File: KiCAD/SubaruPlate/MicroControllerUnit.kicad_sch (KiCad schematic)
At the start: 1 part, among them U5 XIAO-RP2040-DIP

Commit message: SubaruPlateを更新
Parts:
- added BZ1: Buzzer, symbol Device:Buzzer
- added Q1: NMOS, Package_TO_SOT_SMD:SOT-23, symbol Simulation_SPICE:NMOS
- added R5: 750, Resistor_SMD:R_0603_1608Metric_Pad0.98x0.95mm_HandSolder, symbol Device:R
- added R7: 10k, Resistor_SMD:R_0603_1608Metric_Pad0.98x0.95mm_HandSolder, symbol Device:R
- U5: footprint Module:MOUDLE14P-XIAO-DIP-SMD -> Seeed_XIAO:XIAO-RP2040-SMD
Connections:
- net GND: now also Q1.3 (S), R7.1
- net Servo_PWM: now reaches U5.2 (GPIO27/ADC1/A1)
- net Buzzer: now reaches U5.3 (GPIO28/ADC2/A2)
- net Buzzer: now also R5.1
- new net: Q1.2 (G), R5.2, R7.2
- new net: BZ1.2 (-), Q1.1 (D)
- new net +12V: BZ1.1 (+)
- no-connect marks 5 -> 3
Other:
- note added: "アナデジ太郎の回路設計・FETのゲート・ソース間抵抗の決め方"
- note added: "アナデジ太郎の回路設計・FETゲート抵抗の決め方"

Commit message: 後は最終確認
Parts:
- added R13: 600, Resistor_SMD:R_0603_1608Metric_Pad0.98x0.95mm_HandSolder, symbol Device:R
- BZ1: footprint (none) -> Buzzer_Beeper:Buzzer_12x9.5RM7.6
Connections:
- net +12V: now also R13.1; no longer BZ1.1 (+)
- net SPI_CS_MCP2515: now reaches U5.4 (GPIO29/ADC3/A3)
- net +3.3V: no longer names the net of U5.12 (3V3)
- new net: BZ1.1 (+), R13.2
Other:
- note added: "音質に問題があれば，0Ω抵抗で配線→"
- moved on the sheet: BZ1, Q1, R5, R7

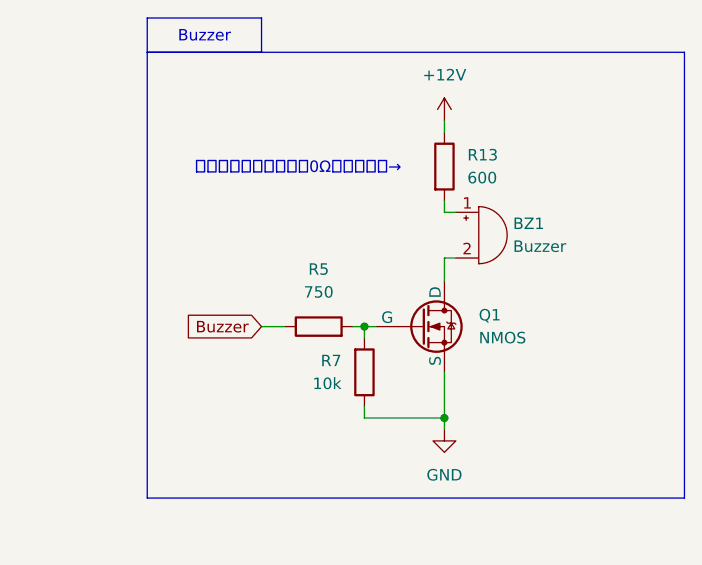
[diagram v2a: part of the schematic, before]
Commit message: 取付穴位置を変更
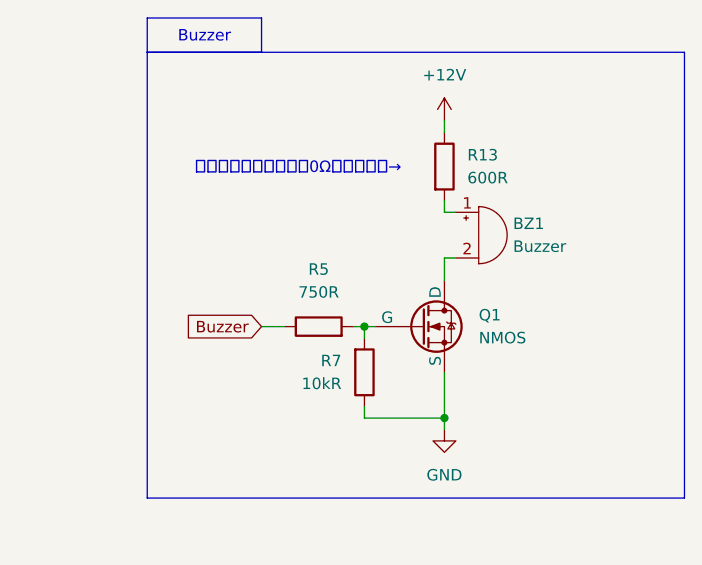
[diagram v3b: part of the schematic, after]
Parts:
- R13: value 600 -> 600R
- R5: value 750 -> 750R
- R7: value 10k -> 10kR
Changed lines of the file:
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@@
 			)
 		)
-		(property "Value" "750"
+		(property "Value" "750R"
 			(at 146.05 52.07 90)
 			(effects
@@
 			)
 		)
-		(property "Value" "600"
+		(property "Value" "600R"
 			(at 162.56 39.3699 0)
 			(effects
@@
 			)
 		)
-		(property "Value" "10k"
+		(property "Value" "10kR"
 			(at 148.59 62.2299 0)
 			(effects

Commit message: ガバーデータ生成
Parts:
- U5: footprint Seeed_XIAO:XIAO-RP2040-SMD -> TSRP_Seeed_XIAO:XIAO-RP2040-SMD
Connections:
- net +12V renamed VIN(12V)
- net SPI_CS: no longer names the net of U5.1 (GPIO26/ADC0/A0)
- net Servo_PWM: no longer names the net of U5.2 (GPIO27/ADC1/A1)
- no-connect marks 3 -> 5
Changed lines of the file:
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@@
+	)
+	(no_connect
+		(at 48.26 36.83)
+	)
+	(no_connect
+		(at 48.26 40.64)
 	)
 	(no_connect
@@
 	(wire
 		(pts
-			(xy 160.02 33.02) (xy 160.02 34.29)
+			(xy 160.02 31.75) (xy 160.02 34.29)
 		)
 		(stroke
@@
 		(pts
 			(xy 151.13 55.88) (xy 151.13 57.15)
+		)
+		(stroke
+			(width 0)
+			(type default)
+		)
+	)
+	(wire
+		(pts
+			(xy 158.75 31.75) (xy 160.02 31.75)
 		)
 		(stroke
@@
 		)
 	)
-	(global_label "Servo_PWM"
-		(shape output)
-		(at 48.26 40.64 180)
+	(global_label "SPI_MISO"
+		(shape input)
+		(at 83.82 52.07 0)
 		(fields_autoplaced yes)
 		(effects
@@
 				(size 1.27 1.27)
 			)
-			(justify right)
+			(justify left)
 		)
 		(property "Intersheetrefs" "${INTERSHEET_REFS}"
-			(at 34.9335 40.64 0)
-			(show_name yes)
-			(effects
-				(font
-					(size 1.27 1.27)
-				)
-				(justify right)
-				(hide yes)
-			)
-		)
-	)
-	(global_label "SPI_MISO"
+			(at 95.4533 52.07 0)
+			(effects
+				(font
+					(size 1.27 1.27)
+				)
+				(justify left)
+				(hide yes)
+			)
+		)
+	)
+	(global_label "I2C_SCL"
 		(shape input)
-		(at 83.82 52.07 0)
+		(at 48.26 55.88 180)
 		(fields_autoplaced yes)
 		(effects
@@
 				(size 1.27 1.27)
 			)
-			(justify left)
+			(justify right)
 		)
 		(property "Intersheetrefs" "${INTERSHEET_REFS}"
-			(at 95.4533 52.07 0)
-			(effects
-				(font
-					(size 1.27 1.27)
-				)
-				(justify left)
-				(hide yes)
-			)
-		)
-	)
-	(global_label "I2C_SCL"
+			(at 37.7153 55.88 0)
+			(effects
+				(font
+					(size 1.27 1.27)
+				)
+				(justify right)
+				(hide yes)
+			)
+		)
+	)
+	(global_label "SPI_CS_MCP2515"
 		(shape input)
-		(at 48.26 55.88 180)
+		(at 48.26 48.26 180)
 		(fields_autoplaced yes)
 		(effects
@@
 		)
 		(property "Intersheetrefs" "${INTERSHEET_REFS}"
-			(at 37.7153 55.88 0)
+			(at 28.9464 48.26 0)
 			(effects
 				(font
@@
 		)
 	)
-	(global_label "SPI_CS_MCP2515"
+	(global_label "I2C_SDA"
 		(shape input)
-		(at 48.26 48.26 180)
+		(at 48.26 52.07 180)
 		(fields_autoplaced yes)
 		(effects
@@
 		)
 		(property "Intersheetrefs" "${INTERSHEET_REFS}"
-			(at 28.9464 48.26 0)
+			(at 37.6548 52.07 0)
 			(effects
 				(font
@@
 		)
 	)
-	(global_label "I2C_SDA"
+	(global_label "Buzzer"
 		(shape input)
-		(at 48.26 52.07 180)
+		(at 139.7 55.88 180)
 		(fields_autoplaced yes)
 		(effects
@@
 		)
 		(property "Intersheetrefs" "${INTERSHEET_REFS}"
-			(at 37.6548 52.07 0)
+			(at 130.3648 55.88 0)
 			(effects
 				(font
@@
 		)
 	)
-	(global_label "Buzzer"
+	(global_label "VIN(12V)"
 		(shape input)
-		(at 139.7 55.88 180)
+		(at 158.75 31.75 180)
 		(fields_autoplaced yes)
 		(effects
@@
 		)
 		(property "Intersheetrefs" "${INTERSHEET_REFS}"
-			(at 130.3648 55.88 0)
-			(effects
-				(font
-					(size 1.27 1.27)
-				)
-				(justify right)
-				(hide yes)
-			)
-		)
-	)
-	(global_label "SPI_CS"
-		(shape input)
-		(at 48.26 36.83 180)
-		(fields_autoplaced yes)
-		(effects
-			(font
-				(size 1.27 1.27)
-			)
-			(justify right)
-		)
-		(property "Intersheetrefs" "${INTERSHEET_REFS}"
-			(at 38.7434 36.83 0)
+			(at 147.5399 31.75 0)
 			(effects
 				(font
@@
 	)
 	(symbol
-		(lib_id "power:+12V")
-		(at 160.02 33.02 0)
-		(unit 1)
-		(exclude_from_sim no)
-		(in_bom yes)
-		(on_board yes)
-		(dnp no)
-		(fields_autoplaced yes)
-		(property "Reference" "#PWR031"
-			(at 160.02 36.83 0)
-			(effects
-				(font
-					(size 1.27 1.27)
-				)
-				(hide yes)
-			)
-		)
-		(property "Value" "+12V"
-			(at 160.02 27.94 0)
-			(effects
-				(font
-					(size 1.27 1.27)
-				)
-			)
-		)
-		(property "Footprint" ""
-			(at 160.02 33.02 0)
-			(effects
-				(font
-					(size 1.27 1.27)
-				)
-				(hide yes)
-			)
-		)
-		(property "Datasheet" ""
-			(at 160.02 33.02 0)
-			(effects
-				(font
-					(size 1.27 1.27)
-				)
-				(hide yes)
-			)
-		)
-		(property "Description" "Power symbol creates a global label with name \"+12V\""
-			(at 160.02 33.02 0)
-			(effects
-				(font
-					(size 1.27 1.27)
-				)
-				(hide yes)
-			)
-		)
-		(pin "1"
-		)
-		(instances
-			(project ""
-				(path "/6c4aa1f5-c08b-4349-85f8-88bb399e711f/68138f6b-698e-4dab-8cce-76242e9c0eb0"
-					(reference "#PWR031")
-					(unit 1)
-				)
-			)
-		)
-	)
-	(symbol
 		(lib_id "Seeed_Studio_XIAO_Series:XIAO-RP2040-DIP")
 		(at 52.07 31.75 0)
@@
 			)
 		)
-		(property "Footprint" "Seeed_XIAO:XIAO-RP2040-SMD"
+		(property "Footprint" "TSRP_Seeed_XIAO:XIAO-RP2040-SMD"
 			(at 66.548 64.008 0)
 			(effects
